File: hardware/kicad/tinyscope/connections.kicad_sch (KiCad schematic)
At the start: 0 parts

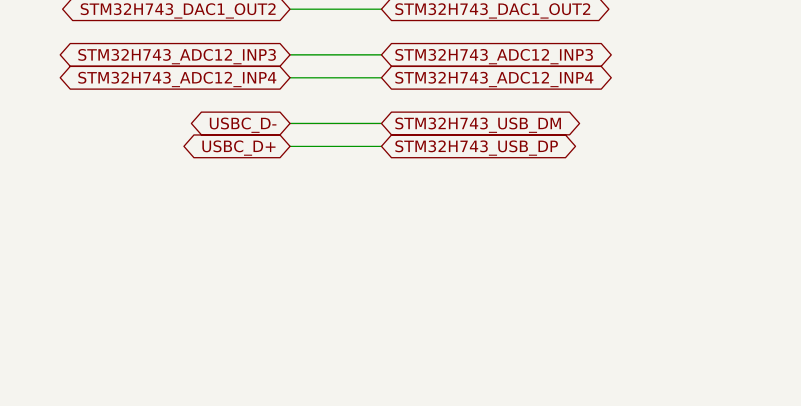
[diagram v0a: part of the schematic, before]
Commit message: fix: hardware: Solves electrical rules warnings and errors #8
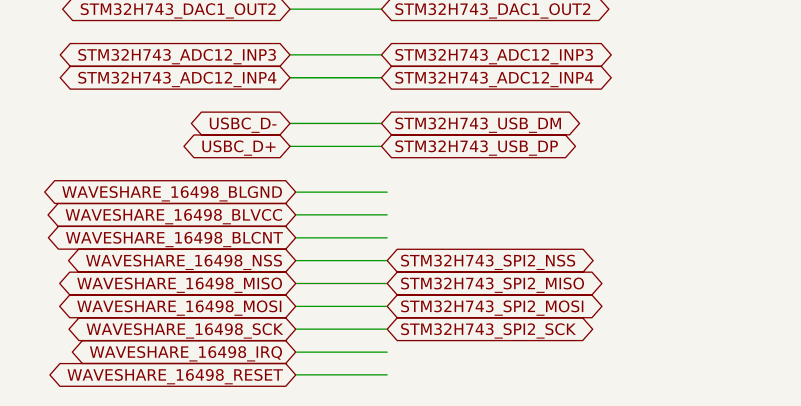
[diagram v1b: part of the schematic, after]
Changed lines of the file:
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@@
+    (stroke (width 0) (type default))
+  )
+  (wire (pts (xy 93.98 160.02) (xy 104.14 160.02))
     (stroke (width 0) (type default))
   )
@@
     (stroke (width 0) (type default))
   )
+  (wire (pts (xy 93.98 152.4) (xy 104.14 152.4))
+    (stroke (width 0) (type default))
+  )
+  (wire (pts (xy 93.98 162.56) (xy 104.14 162.56))
+    (stroke (width 0) (type default))
+  )
+  (wire (pts (xy 93.98 170.18) (xy 104.14 170.18))
+    (stroke (width 0) (type default))
+  )
   (wire (pts (xy 93.345 144.78) (xy 103.505 144.78))
     (stroke (width 0) (type default))
@@
     (stroke (width 0) (type default))
   )
+  (wire (pts (xy 93.98 154.94) (xy 104.14 154.94))
+    (stroke (width 0) (type default))
+  )
   (wire (pts (xy 93.345 119.38) (xy 103.505 119.38))
     (stroke (width 0) (type default))
@@
     (stroke (width 0) (type default))
   )
+  (wire (pts (xy 93.98 165.1) (xy 104.14 165.1))
+    (stroke (width 0) (type default))
+  )
   (wire (pts (xy 93.345 81.28) (xy 103.505 81.28))
     (stroke (width 0) (type default))
   )
+  (wire (pts (xy 93.98 157.48) (xy 104.14 157.48))
+    (stroke (width 0) (type default))
+  )
   (wire (pts (xy 93.345 58.42) (xy 103.505 58.42))
     (stroke (width 0) (type default))
@@
   )
   (wire (pts (xy 93.345 137.16) (xy 103.505 137.16))
+    (stroke (width 0) (type default))
+  )
+  (wire (pts (xy 93.98 167.64) (xy 104.14 167.64))
+    (stroke (width 0) (type default))
+  )
+  (wire (pts (xy 93.98 149.86) (xy 104.14 149.86))
     (stroke (width 0) (type default))
   )
@@
     )
   )
+  (global_label "WAVESHARE_16498_NSS" (shape bidirectional) (at 93.98 157.48 180) (fields_autoplaced)
+    (effects (font (size 1.27 1.27)) (justify right))
+    (property "Intersheetrefs" "${INTERSHEET_REFS}" (at 67.4055 157.48 0)
+      (effects (font (size 1.27 1.27)) (justify right) hide)
+    )
+  )
+  (global_label "STM32H743_SPI2_NSS" (shape bidirectional) (at 104.14 157.48 0) (fields_autoplaced)
+    (effects (font (size 1.27 1.27)) (justify left))
+    (property "Intersheetrefs" "${INTERSHEET_REFS}" (at 129.1421 157.48 0)
+      (effects (font (size 1.27 1.27)) (justify left) hide)
+    )
+  )
   (global_label "STM32H743_GPIO_EXTI8" (shape bidirectional) (at 103.505 91.44 0) (fields_autoplaced)
     (effects (font (size 1.27 1.27)) (justify left))
@@
     )
   )
+  (global_label "STM32H743_SPI2_MOSI" (shape bidirectional) (at 104.14 162.56 0) (fields_autoplaced)
+    (effects (font (size 1.27 1.27)) (justify left))
+    (property "Intersheetrefs" "${INTERSHEET_REFS}" (at 129.9888 162.56 0)
+      (effects (font (size 1.27 1.27)) (justify left) hide)
+    )
+  )
+  (global_label "WAVESHARE_16498_RESET" (shape bidirectional) (at 93.98 170.18 180) (fields_autoplaced)
+    (effects (font (size 1.27 1.27)) (justify right))
+    (property "Intersheetrefs" "${INTERSHEET_REFS}" (at 65.4099 170.18 0)
+      (effects (font (size 1.27 1.27)) (justify right) hide)
+    )
+  )
+  (global_label "STM32H743_SPI2_MISO" (shape bidirectional) (at 104.14 160.02 0) (fields_autoplaced)
+    (effects (font (size 1.27 1.27)) (justify left))
+    (property "Intersheetrefs" "${INTERSHEET_REFS}" (at 129.9888 160.02 0)
+      (effects (font (size 1.27 1.27)) (justify left) hide)
+    )
+  )
   (global_label "STM32H743_GPIO_EXTI0" (shape bidirectional) (at 103.505 96.52 0) (fields_autoplaced)
     (effects (font (size 1.27 1.27)) (justify left))
@@
     )
   )
+  (global_label "WAVESHARE_16498_MOSI" (shape bidirectional) (at 93.98 162.56 180) (fields_autoplaced)
+    (effects (font (size 1.27 1.27)) (justify right))
+    (property "Intersheetrefs" "${INTERSHEET_REFS}" (at 66.5588 162.56 0)
+      (effects (font (size 1.27 1.27)) (justify right) hide)
+    )
+  )
   (global_label "USBC_D-" (shape bidirectional) (at 93.345 142.24 180) (fields_autoplaced)
     (effects (font (size 1.27 1.27)) (justify right))
@@
     )
   )
+  (global_label "WAVESHARE_16498_BLCNT" (shape bidirectional) (at 93.98 154.94 180) (fields_autoplaced)
+    (effects (font (size 1.27 1.27)) (justify right))
+    (property "Intersheetrefs" "${INTERSHEET_REFS}" (at 65.2888 154.94 0)
+      (effects (font (size 1.27 1.27)) (justify right) hide)
+    )
+  )
+  (global_label "WAVESHARE_16498_MISO" (shape bidirectional) (at 93.98 160.02 180) (fields_autoplaced)
+    (effects (font (size 1.27 1.27)) (justify right))
+    (property "Intersheetrefs" "${INTERSHEET_REFS}" (at 66.5588 160.02 0)
+      (effects (font (size 1.27 1.27)) (justify right) hide)
+    )
+  )
   (global_label "ENC6_B" (shape bidirectional) (at 93.345 119.38 180) (fields_autoplaced)
     (effects (font (size 1.27 1.27)) (justify right))
@@
     )
   )
+  (global_label "WAVESHARE_16498_BLVCC" (shape bidirectional) (at 93.98 152.4 180) (fields_autoplaced)
+    (effects (font (size 1.27 1.27)) (justify right))
+    (property "Intersheetrefs" "${INTERSHEET_REFS}" (at 65.2283 152.4 0)
+      (effects (font (size 1.27 1.27)) (justify right) hide)
+    )
+  )
   (global_label "ENC3_SW" (shape bidirectional) (at 93.345 91.44 180) (fields_autoplaced)
     (effects (font (size 1.27 1.27)) (justify right))
@@
     )
   )
+  (global_label "WAVESHARE_16498_SCK" (shape bidirectional) (at 93.98 165.1 180) (fields_autoplaced)
+    (effects (font (size 1.27 1.27)) (justify right))
+    (property "Intersheetrefs" "${INTERSHEET_REFS}" (at 67.4055 165.1 0)
+      (effects (font (size 1.27 1.27)) (justify right) hide)
+    )
+  )
   (global_label "STM32H743_DAC1_OUT2" (shape bidirectional) (at 93.345 129.54 180) (fields_autoplaced)
     (effects (font (size 1.27 1.27)) (justify right))
@@
     )
   )
+  (global_label "WAVESHARE_16498_IRQ" (shape bidirectional) (at 93.98 167.64 180) (fields_autoplaced)
+    (effects (font (size 1.27 1.27)) (justify right))
+    (property "Intersheetrefs" "${INTERSHEET_REFS}" (at 67.9497 167.64 0)
+      (effects (font (size 1.27 1.27)) (justify right) hide)
+    )
+  )
   (global_label "STM32H743_DAC1_OUT1" (shape bidirectional) (at 93.345 127 180) (fields_autoplaced)
     (effects (font (size 1.27 1.27)) (justify right))
@@
     )
   )
+  (global_label "STM32H743_SPI2_SCK" (shape bidirectional) (at 104.14 165.1 0) (fields_autoplaced)
+    (effects (font (size 1.27 1.27)) (justify left))
+    (property "Intersheetrefs" "${INTERSHEET_REFS}" (at 129.1421 165.1 0)
+      (effects (font (size 1.27 1.27)) (justify left) hide)
+    )
+  )
   (global_label "STM32H743_GPIO_EXTI1" (shape bidirectional) (at 103.505 101.6 0) (fields_autoplaced)
     (effects (font (size 1.27 1.27)) (justify left))
@@
     )
   )
+  (global_label "WAVESHARE_16498_BLGND" (shape bidirectional) (at 93.98 149.86 180) (fields_autoplaced)
+    (effects (font (size 1.27 1.27)) (justify right))
+    (property "Intersheetrefs" "${INTERSHEET_REFS}" (at 64.9864 149.86 0)
+      (effects (font (size 1.27 1.27)) (justify right) hide)
+    )
+  )

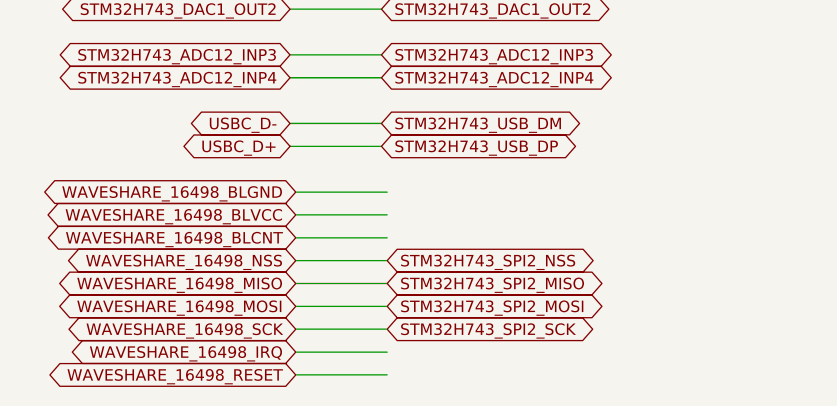
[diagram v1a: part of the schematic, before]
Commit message: feat: hardware: Maps waveshare display connections
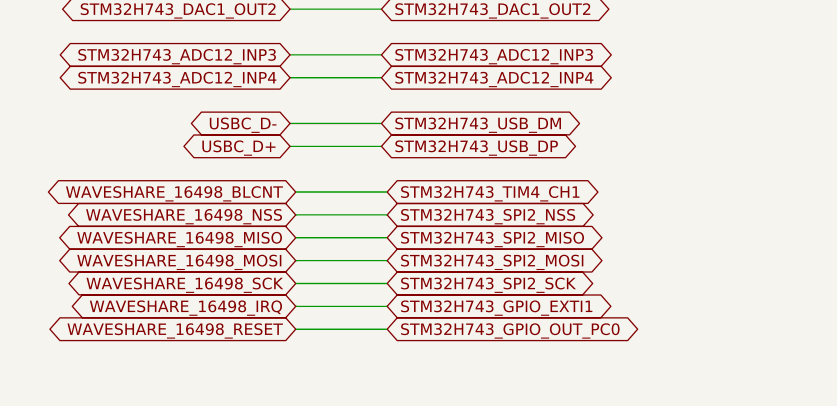
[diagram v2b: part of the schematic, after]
